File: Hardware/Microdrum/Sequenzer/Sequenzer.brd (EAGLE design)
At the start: 100 x 80 mm, 20 parts

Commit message: Langsam nimmt es Form an
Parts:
- removed SLED_MX, TLED_MX: 74HCT138N, 74xx-eu:DIL16
- added LED_MX1, LED_MX2: 74HCT138N, 74xx-eu:DIL16
- moved SV1 27.4 mm to (49.5, 53.3)
- moved TLED1 11.4 mm to (5.08, 43.2)
- moved TLED2 11.4 mm to (17.8, 43.2)
- moved TLED3 11.4 mm to (30.5, 43.2)
- moved TLED4 11.4 mm to (43.2, 43.2)
- moved TLED5 11.4 mm to (55.9, 43.2)
- moved TLED6 11.4 mm to (68.6, 43.2)
- moved TLED7 11.4 mm to (81.3, 43.2)
- moved TLED8 11.4 mm to (94.0, 43.2)
- moved S_MX 1.27 mm to (50.8, 14.0)
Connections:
- net S1 renamed N$11
- net S2 renamed N$10
- net S3 renamed N$9
- net S4 renamed N$8
- net S5 renamed N$7
- net S6 renamed N$6
- net S7 renamed N$5
- net S8 renamed N$4
- removed net 1: SLED_MX.1, SV1.7, S_MX.1, TLED_MX.1
- removed net 2: SLED_MX.2, SV1.5, S_MX.2, TLED_MX.2
- removed net 3: SLED_MX.3, SV1.3, S_MX.3, TLED_MX.3
- removed net SLED1: S1.-, SLED_MX.7
- removed net SLED2: S2.-, SLED_MX.9
- removed net SLED3: S3.-, SLED_MX.10
- removed net SLED4: S4.-, SLED_MX.11
- removed net SLED5: S5.-, SLED_MX.12
- removed net SLED6: S6.-, SLED_MX.13
- removed net SLED7: S7.-, SLED_MX.14
- removed net SLED8: S8.-, SLED_MX.15
- removed net SLED_EN: SLED_MX.6, SV1.8
- removed net TLED1: TLED1.K, TLED_MX.7
- removed net TLED2: TLED2.K, TLED_MX.9
- removed net TLED3: TLED3.K, TLED_MX.10
- removed net TLED4: TLED4.K, TLED_MX.11
- removed net TLED5: TLED5.K, TLED_MX.12
- removed net TLED6: TLED6.K, TLED_MX.13
- removed net TLED7: TLED7.K, TLED_MX.14
- removed net TLED8: TLED8.K, TLED_MX.15
- new net N$1: LED_MX1.1, LED_MX2.1, S_MX.1
- new net N$12: LED_MX1.7, TLED1.K
- new net N$13: LED_MX1.9, S1.-
- new net N$14: LED_MX1.10, TLED2.K
- new net N$15: LED_MX1.11, S2.-
- new net N$16: LED_MX1.12, TLED3.K
- new net N$17: LED_MX1.13, S3.-
- new net N$18: LED_MX1.14, TLED4.K
- new net N$19: LED_MX1.15, S4.-
- new net N$2: LED_MX1.2, LED_MX2.2, S_MX.2
- new net N$3: LED_MX1.3, LED_MX2.3, S_MX.3
- net GND: now also LED_MX1.4, LED_MX1.5, LED_MX1.8, LED_MX2.4, LED_MX2.5, LED_MX2.8; no longer SLED_MX.4, SLED_MX.5, SLED_MX.8, TLED_MX.4, TLED_MX.5, TLED_MX.8
- net TLED_EN: now also LED_MX2.6; no longer SV1.10, TLED_MX.6
- net VCC: now also LED_MX1.16, LED_MX2.16, SV1.1; no longer SLED_MX.16, TLED_MX.16
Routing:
- net N$1: track 0.00 -> 129.1 mm
- net N$2: track 0.00 -> 123.3 mm
- net N$3: track 0.00 -> 103.3 mm
- net SLED8: track 50.6 -> 0.00 mm
- net SLED1: track 50.6 -> 0.00 mm
- net SLED2: track 35.3 -> 0.00 mm
- net SLED7: track 35.3 -> 0.00 mm
- net N$19: track 0.00 -> 31.8 mm
- net SLED6: track 25.2 -> 0.00 mm
- net N$12: track 0.00 -> 23.2 mm
- net N$18: track 0.00 -> 21.4 mm
- net N$13: track 0.00 -> 21.4 mm
- net N$17: track 0.00 -> 20.6 mm
- net SLED3: track 16.8 -> 0.00 mm
- net N$15: track 0.00 -> 14.5 mm
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
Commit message: Vorläufig fertiges Layout
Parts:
- moved LED_MX1 7.01 mm to (24.8, 46.4)
- moved LED_MX2 7.01 mm to (75.6, 46.4)
- moved S6 6.38 mm to (69.2, 24.1)
- moved S7 6.38 mm to (81.9, 24.1)
- moved TLED6 6.38 mm to (69.2, 36.8)
- moved TLED7 6.38 mm to (81.9, 36.8)
- moved S_MX 6.38 mm to (51.4, 7.62)
- moved S1 6.38 mm to (5.71, 24.1)
- moved S2 6.38 mm to (18.4, 24.1)
- moved S3 6.38 mm to (31.1, 24.1)
- moved S4 6.38 mm to (43.8, 24.1)
- moved S5 6.38 mm to (56.5, 24.1)
- moved S8 6.38 mm to (94.6, 24.1)
- moved TLED1 6.38 mm to (5.71, 36.8)
- moved TLED2 6.38 mm to (18.4, 36.8)
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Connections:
- net N$12 renamed TLED1
- net N$13 renamed SLED1
- net N$14 renamed TLED2
- net N$15 renamed SLED2
- net N$16 renamed TLED3
- net N$17 renamed SLED
- net N$18 renamed TLED4
- net N$19 renamed SLED4
- removed net N$1: LED_MX1.1, LED_MX2.1, S_MX.1
- removed net N$2: LED_MX1.2, LED_MX2.2, S_MX.2
- removed net N$3: LED_MX1.3, LED_MX2.3, S_MX.3
- removed net TLED_EN: LED_MX2.6
- new net 1: LED_MX1.1, LED_MX2.1, SV1.5, S_MX.1
- new net 2: LED_MX1.2, LED_MX2.2, SV1.7, S_MX.2
- new net 3: LED_MX1.3, LED_MX2.3, SV1.9, S_MX.3
- new net MX1EN: LED_MX1.6, SV1.8
- new net MX2EN: LED_MX2.6, SV1.4
- new net SLED5: LED_MX2.9, S5.-
- new net SLED6: LED_MX2.11, S6.-
- new net SLED7: LED_MX2.13, S7.-
- new net SLED8: LED_MX2.15, S8.-
- new net TLED5: LED_MX2.7, TLED5.K
- new net TLED6: LED_MX2.10, TLED6.K
- new net TLED7: LED_MX2.12, TLED7.K
- new net TLED8: LED_MX2.14, TLED8.K
- net GND: now also SV1.1; no longer SV1.2
- net VCC: now also SV1.2; no longer SV1.1
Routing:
- net 1: track 0.00 -> 211.8 mm, vias 0 -> 2
- net 2: track 0.00 -> 203.7 mm
- net 3: track 0.00 -> 202.0 mm
- net N$1: track 129.1 -> 0.00 mm
- net N$2: track 123.3 -> 0.00 mm
- net N$3: track 103.3 -> 0.00 mm
- net GND: track 151.1 -> 208.0 mm
- net MX2EN: track 0.00 -> 33.3 mm, vias 0 -> 2
- net MX1EN: track 0.00 -> 32.1 mm
- net SLED8: track 0.00 -> 27.2 mm
- net VCC: track 0.00 -> 25.4 mm, vias 0 -> 4
- net TLED5: track 0.00 -> 23.3 mm
- net SLED5: track 0.00 -> 22.5 mm
- net TLED8: track 0.00 -> 20.7 mm
- net SLED7: track 0.00 -> 20.4 mm
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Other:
- board size 100 x 80 mm -> 100.6 x 59.7 mm
- board text added: "Microdrum"
- board text added: "by MaZderMind"

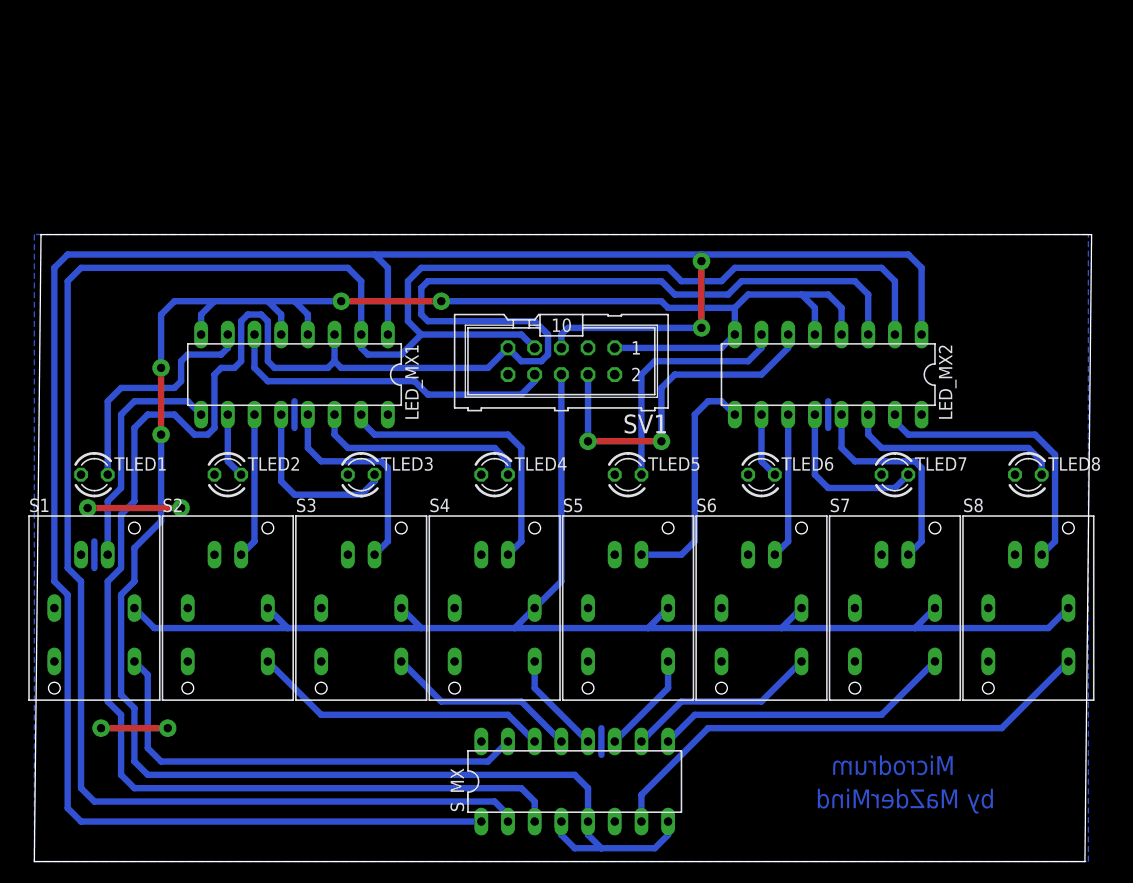
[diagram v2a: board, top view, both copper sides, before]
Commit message: Width wieder zurückgeändert, Dimension begradigt
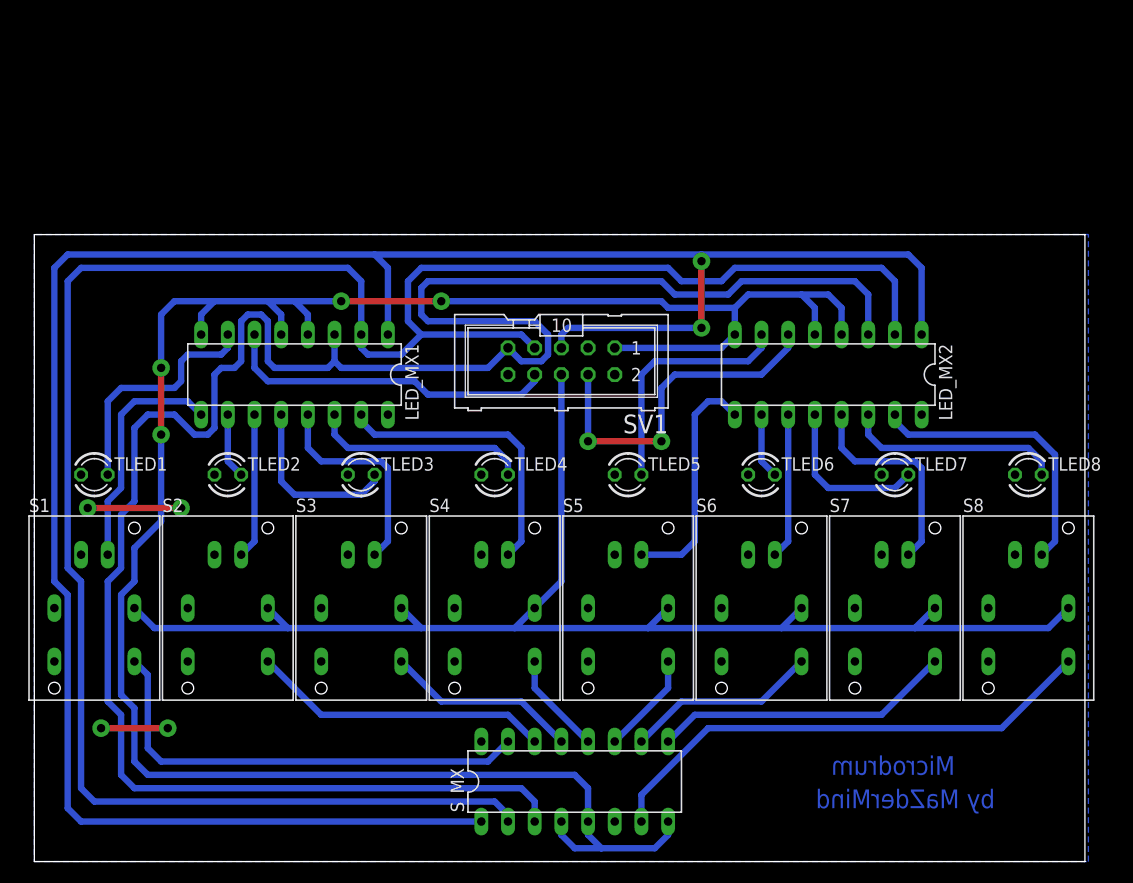
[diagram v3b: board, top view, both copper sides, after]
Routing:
- net VCC: track 25.4 -> 15.2 mm
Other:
- board size 100.6 x 59.7 mm -> 100 x 59.7 mm
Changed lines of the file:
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@@
 <grid distance="0.025" unitdist="inch" unit="inch" style="lines" multiple="1" display="yes" altdistance="0.025" altunitdist="inch" altunit="inch"/>
 <layers>
-<layer number="1" name="Top" color="4" fill="1" visible="yes" active="yes"/>
+<layer number="1" name="Top" color="4" fill="1" visible="no" active="yes"/>
 <layer number="16" name="Bottom" color="1" fill="1" visible="yes" active="yes"/>
 <layer number="17" name="Pads" color="2" fill="1" visible="yes" active="yes"/>
 <layer number="18" name="Vias" color="2" fill="1" visible="yes" active="yes"/>
-<layer number="19" name="Unrouted" color="6" fill="1" visible="yes" active="yes"/>
+<layer number="19" name="Unrouted" color="6" fill="1" visible="no" active="yes"/>
 <layer number="20" name="Dimension" color="15" fill="1" visible="yes" active="yes"/>
-<layer number="21" name="tPlace" color="7" fill="1" visible="yes" active="yes"/>
-<layer number="22" name="bPlace" color="7" fill="1" visible="yes" active="yes"/>
-<layer number="23" name="tOrigins" color="15" fill="1" visible="yes" active="yes"/>
-<layer number="24" name="bOrigins" color="15" fill="1" visible="yes" active="yes"/>
+<layer number="21" name="tPlace" color="7" fill="1" visible="no" active="yes"/>
+<layer number="22" name="bPlace" color="7" fill="1" visible="no" active="yes"/>
+<layer number="23" name="tOrigins" color="15" fill="1" visible="no" active="yes"/>
+<layer number="24" name="bOrigins" color="15" fill="1" visible="no" active="yes"/>
 <layer number="25" name="tNames" color="7" fill="1" visible="no" active="yes"/>
 <layer number="26" name="bNames" color="7" fill="1" visible="no" active="yes"/>
@@
 <layer number="48" name="Document" color="7" fill="1" visible="no" active="yes"/>
 <layer number="49" name="Reference" color="7" fill="1" visible="no" active="yes"/>
-<layer number="51" name="tDocu" color="7" fill="1" visible="yes" active="yes"/>
-<layer number="52" name="bDocu" color="7" fill="1" visible="yes" active="yes"/>
+<layer number="51" name="tDocu" color="7" fill="1" visible="no" active="yes"/>
+<layer number="52" name="bDocu" color="7" fill="1" visible="no" active="yes"/>
 <layer number="91" name="Nets" color="2" fill="1" visible="no" active="no"/>
 <layer number="92" name="Busses" color="1" fill="1" visible="no" active="no"/>
@@
 <plain>
 <wire x1="0" y1="0" x2="100" y2="0" width="0" layer="20"/>
-<wire x1="100" y1="0" x2="100.635" y2="59.68" width="0" layer="20"/>
-<wire x1="100.635" y1="59.68" x2="0.635" y2="59.68" width="0" layer="20"/>
-<wire x1="0.635" y1="59.68" x2="0" y2="0" width="0" layer="20"/>
+<wire x1="100" y1="0" x2="100" y2="59.68" width="0" layer="20"/>
+<wire x1="100" y1="59.68" x2="0" y2="59.68" width="0" layer="20"/>
+<wire x1="0" y1="59.68" x2="0" y2="0" width="0" layer="20"/>
 <text x="87.63" y="8.255" size="1.778" layer="16" font="vector" rot="MR0">Microdrum</text>
 <text x="91.44" y="5.08" size="1.778" layer="16" font="vector" rot="MR0">by MaZderMind</text>
@@
 <contactref element="TLED7" pad="A"/>
 <contactref element="TLED8" pad="A"/>
-<polygon width="0.6096" layer="16" isolate="0.4064">
+<polygon width="0.4064" layer="16" isolate="0.4064">
 <vertex x="0" y="0"/>
 <vertex x="100.33" y="0"/>
@@
 <via x="13.97" y="33.655" extent="1-16" drill="0.8" diameter="1.6764" shape="square"/>
 <wire x1="5.08" y1="33.655" x2="13.97" y2="33.655" width="0.6096" layer="1"/>
-<wire x1="53.975" y1="12.7" x2="53.975" y2="10.16" width="0.6096" layer="16"/>
-<wire x1="75.565" y1="43.815" x2="75.565" y2="41.275" width="0.6096" layer="16"/>
-<wire x1="24.765" y1="43.815" x2="24.765" y2="41.275" width="0.6096" layer="16"/>
-<wire x1="5.715" y1="30.48" x2="5.715" y2="27.94" width="0.6096" layer="16"/>
 </signal>
 <signal name="S_SENSE">
